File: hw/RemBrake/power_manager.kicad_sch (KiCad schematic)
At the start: 23 parts, among them IC1 LTC2943IDD#TRPBF, J3 Screw_Terminal_01x02, J4 Conn_01x03_MountingPin, Q1 BC337, Q2 BC847, U2 MAX40200AUK, U9 MAX40200AUK

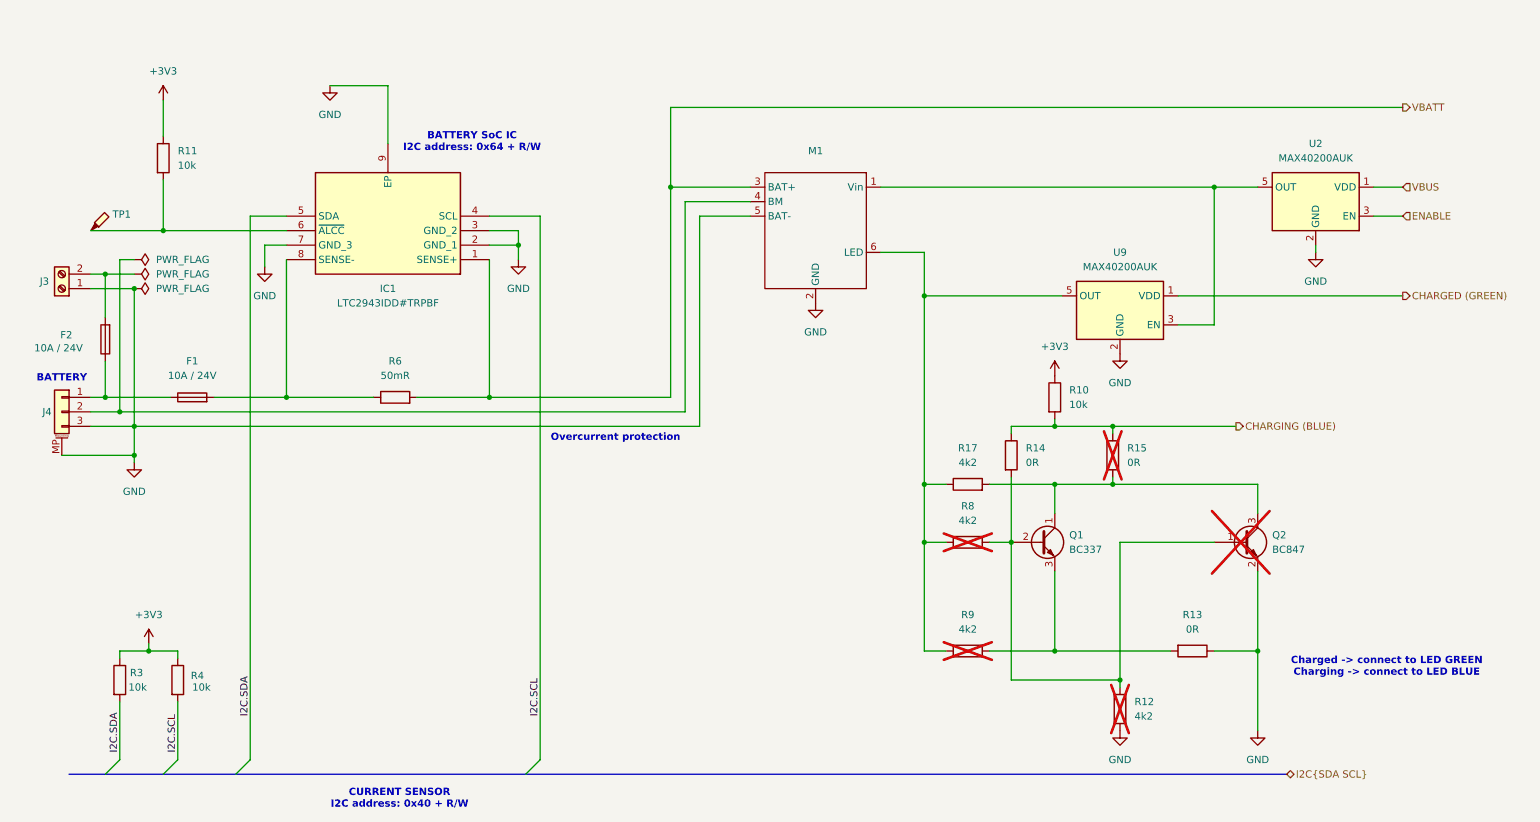
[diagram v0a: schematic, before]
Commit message: project renamed, schematics changed based on breakout boards notes and created new layout with better connectors
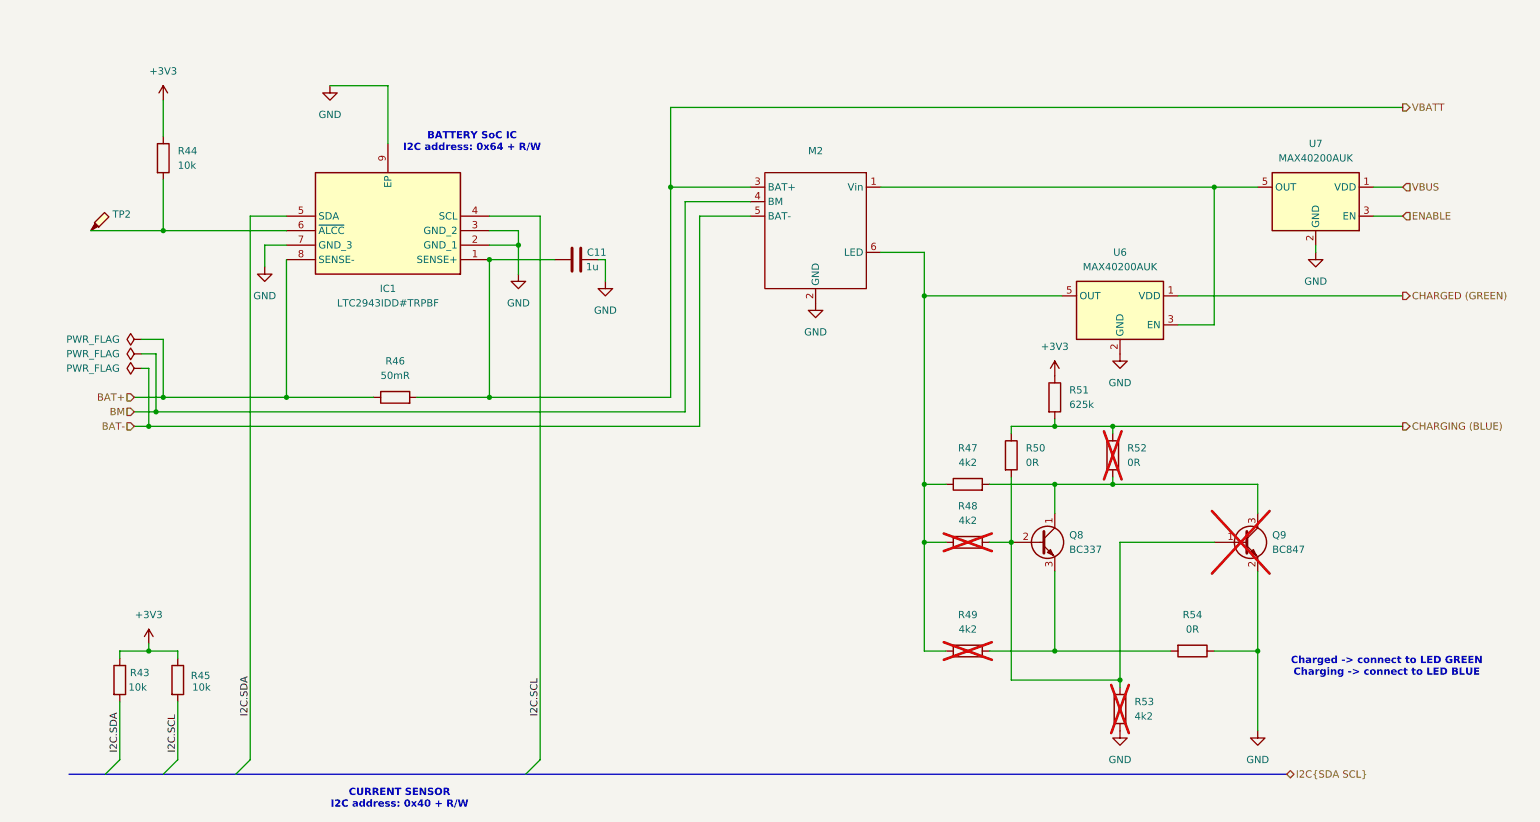
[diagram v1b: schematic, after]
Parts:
- removed F1, F2: 10A / 24V, Fuse:Fuse_1206_3216Metric_Pad1.42x1.75mm_HandSolder, symbol Device:Fuse
- removed J3: Screw_Terminal_01x02, TerminalBlock_Phoenix:TerminalBlock_Phoenix_MKDS-1,5-2_1x02_P5.00mm_Horizontal, symbol Connector:Screw_Terminal_01x02
- removed J4: Conn_01x03_MountingPin, Connector_JST:JST_XH_S3B-XH-SM4-TB_1x03-1MP_P2.50mm_Horizontal, symbol Connector_Generic_MountingPin:Conn_01x03_MountingPin
- removed M1: ~, chinese_modules:USBC_charger, symbol chinese_modules:USBC_charger
- added C11: 1u, Capacitor_SMD:C_0805_2012Metric_Pad1.18x1.45mm_HandSolder, symbol Device:C
- added M2: ~, chinese_modules:USBC_charger, symbol chinese_modules:USBC_charger
- R51: renamed from R10; value 10k -> 625k
- TP2: renamed from TP1; footprint (none) -> TestPoint:TestPoint_Pad_1.5x1.5mm
- renumbered Q1 to Q8, Q2 to Q9, R3 to R43, R11 to R44, R4 to R45, R6 to R46, R17 to R47, R8 to R48, R9 to R49, R14 to R50, R15 to R52, R12 to R53, R13 to R54, U9 to U6, U2 to U7
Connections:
- net GND: now also C11.1, M2.2 (GND)
- net VBATT: now also C11.2, M2.3 (BAT+)
- net BAT+: now reaches IC1.8 (SENSE-), R46.1
- net at R47.1, R48.1, R49.1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: now also M2.6 (LED)
- net at U6.3 (EN), U7.5 (OUT): now also M2.1 (Vin)
- new net BAT-: M2.5 (BAT-)
- new net BM: M2.4 (BM)
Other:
- note removed: "BATTERY"
- note removed: "Overcurrent protection"

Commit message: added few components to fix indicator LED undefined cathode voltage and added vbus divider to match MCU voltage level
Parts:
- added R55, R57: 10k, Resistor_SMD:R_0805_2012Metric_Pad1.20x1.40mm_HandSolder, symbol Device:R
- renumbered R43 to R44, R44 to R45, R45 to R46, R46 to R47, R47 to R48, R48 to R49, R49 to R50, R50 to R51, R51 to R52, R52 to R53, R53 to R54, R54 to R56
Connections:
- net +3V3: now also R55.1
- net CHARGED (GREEN): now also R55.2
- net at M2.1 (Vin), U7.5 (OUT): now also R57.1; no longer U6.3 (EN)
- new net: R57.2, U6.3 (EN)

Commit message: updated date and revision in the schematics
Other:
- company: (none) -> Pacner Bros Tech
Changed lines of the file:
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@@
 	(title_block
 		(title "Power Manager")
-		(date "2024-12-15")
-		(rev "1.0")
+		(date "2025-02-23")
+		(rev "2.0")
+		(company "Pacner Bros Tech")
 	)
 	(text "CURRENT SENSOR\nI2C address: 0x40 + R/W"

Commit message: updated annotation
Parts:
- C11: value 1u -> 1uF
- Q9: now left out of the parts list
- R51: renamed from R47; value 50mR -> 10mR
- R52: renamed from R48; value 4k2 -> 5k
- R53: renamed from R49; value 4k2 -> 5k; now left out of the parts list
- R54: renamed from R50; value 4k2 -> 5k; now left out of the parts list
- R56: renamed from R52; value 625k -> 590k
- R57: renamed from R53; now left out of the parts list
- R58: renamed from R54; value 4k2 -> 0R; now left out of the parts list
- renumbered R44 to R48, R45 to R49, R46 to R50, R51 to R55, R55 to R59, R56 to R60, R57 to R61, TP2 to TP4

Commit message: added 555 counter output divider to adjust to 3v3 voltage level
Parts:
- renumbered R48 to R50, R49 to R51, R50 to R52, R51 to R53, R52 to R54, R53 to R55, R54 to R56, R55 to R57, R56 to R58, R57 to R59, R58 to R60, R59 to R61, R60 to R62, R61 to R63

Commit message: fixed bugs with LED reverse current leakage and beeper deterministic startup delay
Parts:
- R51: renamed from R50; now not fitted
- R52: renamed from R51; now not fitted
- R53: renamed from R52; now not fitted
- R55: renamed from R54; value 5k -> 5k1
- R59: renamed from R58; value 590k -> 10k
- renumbered R53 to R54, R55 to R56, R56 to R57, R57 to R58, R59 to R60, R60 to R61, R61 to R62, R62 to R63, R63 to R64
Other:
- note added: "Note: the ALCC pin can be set to output, so, when the LTC2943 is started for the first time from the assembly the 1V8 output gets to the 3V3 power line"

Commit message: replaced optocoupler with transistor and loaded components in the pcb sheet
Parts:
- renumbered C11 to C13, Q8 to Q10, Q9 to Q11, R51 to R55, R52 to R56, R53 to R57, R54 to R58, R55 to R59, R56 to R60, R57 to R61, R58 to R62, R59 to R63, R60 to R64, R61 to R65, R62 to R66, R63 to R67, R64 to R68, U6 to U7, U7 to U8
